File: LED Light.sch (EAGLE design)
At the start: 17 parts, among them J1 AVR_SPI_PRG_6NS, U1 Tiny85-20-SMT

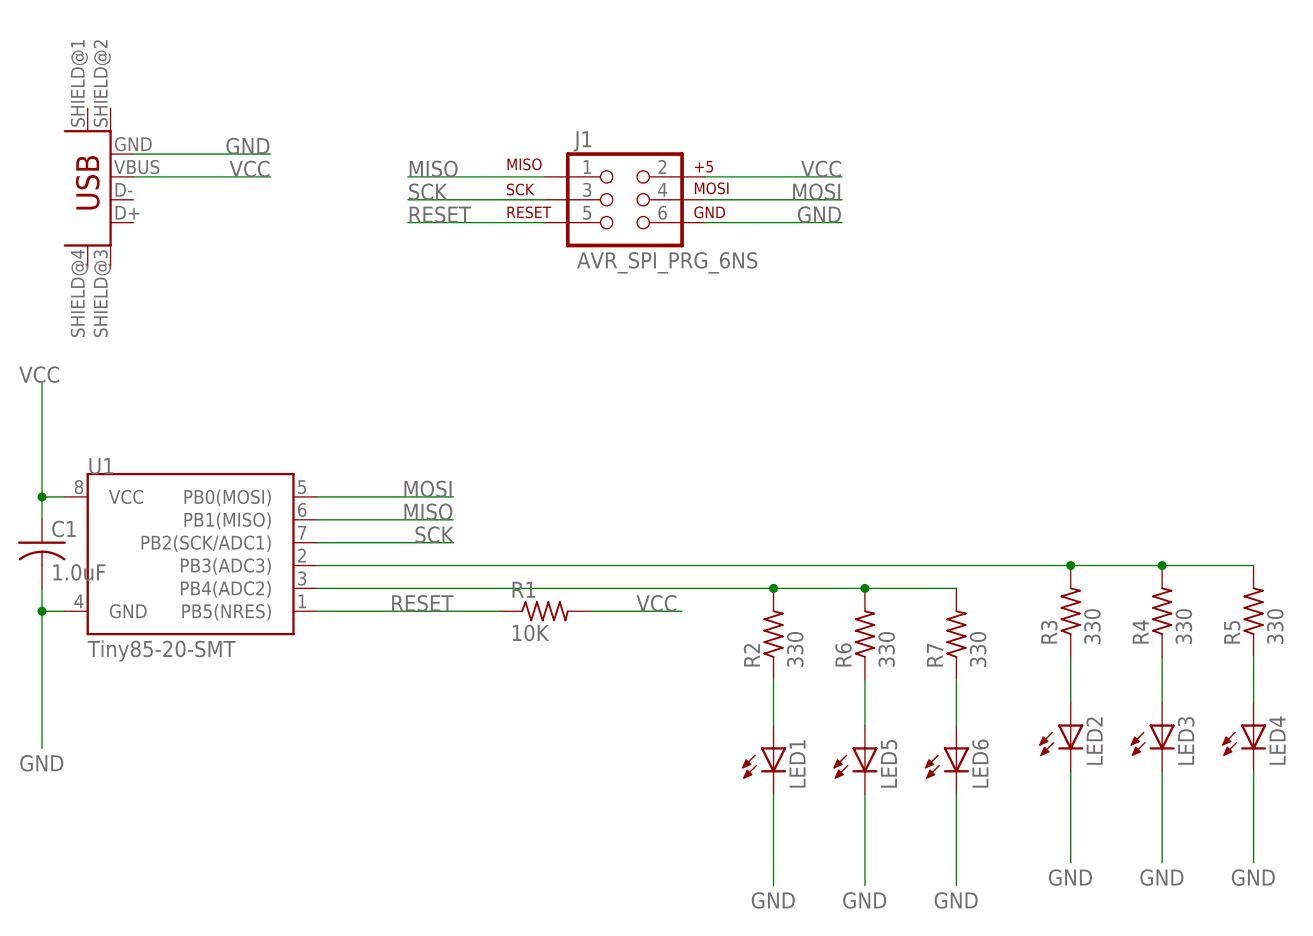
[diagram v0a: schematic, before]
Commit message: Light-bulb-shaped board, reverse-mount LEDs, and SMT AVR ISP header.
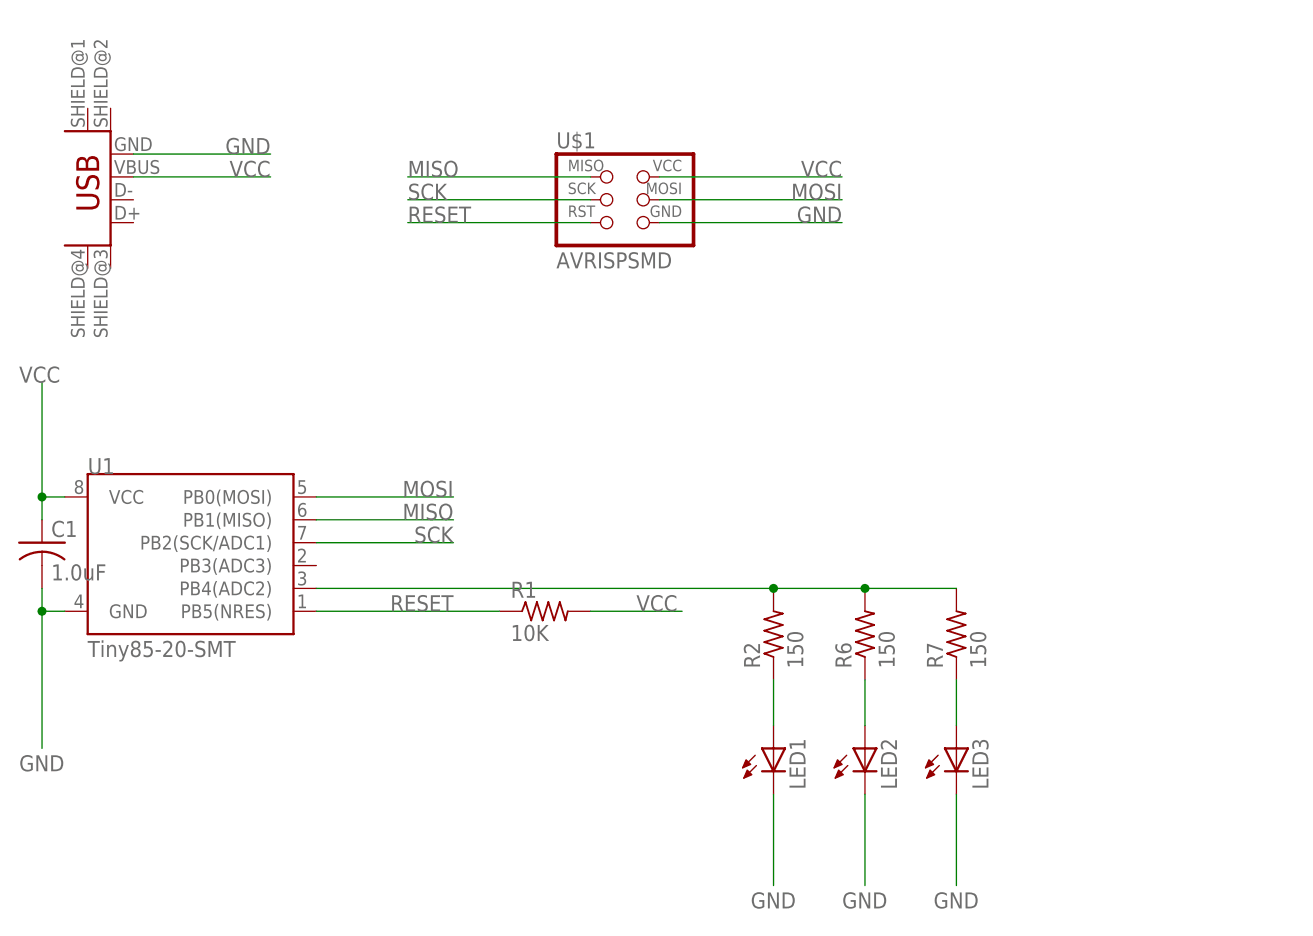
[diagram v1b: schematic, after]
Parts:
- removed J1: AVR_SPI_PRG_6NS, SparkFun-Connectors:AVR_SPI_PRG_6NS
- removed LED4, LED5, LED6: (no value), led:LEDSMT1206
- removed R3, R4, R5: 330, rcl:R-US_R1206
- added U$1: AVRISPSMD, fab:AVRISPSMD
- LED1, LED2, LED3: device led:LEDSMT1206 -> led:LEDTOPLED-SANTANA
- R2, R6, R7: value 330 -> 150
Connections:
- removed net N$2: R3.2, R4.2, R5.2, U1.PB3(ADC3)
- removed net N$4: LED2.A, R3.1
- removed net N$7: LED3.A, R4.1
- removed net N$8: LED4.A, R5.1
- net GND: now also U$1.GND; no longer J1.6, LED4.C, LED5.C, LED6.C
- net MISO: now also U$1.MISO; no longer J1.1
- net MOSI: now also U$1.MOSI; no longer J1.4
- net N$5: now also LED3.A; no longer LED6.A
- net N$6: now also LED2.A; no longer LED5.A
- net RESET: now also U$1.RST; no longer J1.5
- net SCK: now also U$1.SCK; no longer J1.3
- net VCC: now also U$1.VCC; no longer J1.2
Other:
- moved on the sheet: LED2, LED3
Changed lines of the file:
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@@
 <parts>
 <part name="U1" library="SparkFun-DigitalIC" deviceset="ATTINY45" device="TINY85-20-SMT" value="Tiny85-20-SMT"/>
-<part name="J1" library="SparkFun-Connectors" deviceset="AVR_SPI_PRG_6" device="NS"/>
 <part name="R1" library="rcl" deviceset="R-US_" device="R1206" value="10K"/>
-<part name="R2" library="rcl" deviceset="R-US_" device="R1206" value="330"/>
-<part name="R3" library="rcl" deviceset="R-US_" device="R1206" value="330"/>
-<part name="LED1" library="led" deviceset="LED" device="SMT1206"/>
-<part name="LED2" library="led" deviceset="LED" device="SMT1206"/>
+<part name="R2" library="rcl" deviceset="R-US_" device="R1206" value="150"/>
 <part name="JP1" library="fab" deviceset="USB_MINIB" device=""/>
 <part name="C1" library="rcl" deviceset="C-US" device="C1206" value="1.0uF"/>
-<part name="R4" library="rcl" deviceset="R-US_" device="R1206" value="330"/>
-<part name="LED3" library="led" deviceset="LED" device="SMT1206"/>
-<part name="R5" library="rcl" deviceset="R-US_" device="R1206" value="330"/>
-<part name="LED4" library="led" deviceset="LED" device="SMT1206"/>
-<part name="R6" library="rcl" deviceset="R-US_" device="R1206" value="330"/>
-<part name="R7" library="rcl" deviceset="R-US_" device="R1206" value="330"/>
-<part name="LED5" library="led" deviceset="LED" device="SMT1206"/>
-<part name="LED6" library="led" deviceset="LED" device="SMT1206"/>
+<part name="R6" library="rcl" deviceset="R-US_" device="R1206" value="150"/>
+<part name="R7" library="rcl" deviceset="R-US_" device="R1206" value="150"/>
+<part name="LED1" library="led" deviceset="LED" device="TOPLED-SANTANA"/>
+<part name="LED2" library="led" deviceset="LED" device="TOPLED-SANTANA"/>
+<part name="LED3" library="led" deviceset="LED" device="TOPLED-SANTANA"/>
+<part name="U$1" library="fab" deviceset="AVRISP" device="SMD"/>
 </parts>
 <sheets>
@@
 <instances>
 <instance part="U1" gate="G$1" x="27.94" y="38.1"/>
-<instance part="J1" gate="G$1" x="73.66" y="78.74"/>
 <instance part="R1" gate="G$1" x="66.04" y="33.02"/>
 <instance part="R2" gate="G$1" x="91.44" y="30.48" rot="R90"/>
-<instance part="R3" gate="G$1" x="124.46" y="33.02" rot="R90"/>
-<instance part="LED1" gate="G$1" x="91.44" y="17.78"/>
-<instance part="LED2" gate="G$1" x="124.46" y="20.32"/>
 <instance part="JP1" gate="G$1" x="17.78" y="78.74" rot="R180"/>
 <instance part="C1" gate="G$1" x="10.16" y="40.64"/>
-<instance part="R4" gate="G$1" x="134.62" y="33.02" rot="R90"/>
-<instance part="LED3" gate="G$1" x="134.62" y="20.32"/>
-<instance part="R5" gate="G$1" x="144.78" y="33.02" rot="R90"/>
-<instance part="LED4" gate="G$1" x="144.78" y="20.32"/>
 <instance part="R6" gate="G$1" x="101.6" y="30.48" rot="R90"/>
 <instance part="R7" gate="G$1" x="111.76" y="30.48" rot="R90"/>
-<instance part="LED5" gate="G$1" x="101.6" y="17.78"/>
-<instance part="LED6" gate="G$1" x="111.76" y="17.78"/>
+<instance part="LED1" gate="G$1" x="91.44" y="17.78"/>
+<instance part="LED2" gate="G$1" x="101.6" y="17.78"/>
+<instance part="LED3" gate="G$1" x="111.76" y="17.78"/>
+<instance part="U$1" gate="G$1" x="73.66" y="78.74"/>
 </instances>
 <busses>
@@
 <net name="VCC" class="0">
 <segment>
-<pinref part="J1" gate="G$1" pin="2"/>
-<wire x1="83.82" y1="81.28" x2="99.06" y2="81.28" width="0.1524" layer="91"/>
+<wire x1="78.74" y1="81.28" x2="99.06" y2="81.28" width="0.1524" layer="91"/>
 <label x="99.06" y="81.28" size="1.778" layer="95" rot="MR0"/>
+<pinref part="U$1" gate="G$1" pin="VCC"/>
 </segment>
 <segment>
@@
 <net name="MOSI" class="0">
 <segment>
-<pinref part="J1" gate="G$1" pin="4"/>
-<wire x1="83.82" y1="78.74" x2="99.06" y2="78.74" width="0.1524" layer="91"/>
+<wire x1="78.74" y1="78.74" x2="99.06" y2="78.74" width="0.1524" layer="91"/>
 <label x="99.06" y="78.74" size="1.778" layer="95" rot="MR0"/>
+<pinref part="U$1" gate="G$1" pin="MOSI"/>
 </segment>
 <segment>
@@
 <net name="GND" class="0">
 <segment>
-<pinref part="J1" gate="G$1" pin="6"/>
-<wire x1="83.82" y1="76.2" x2="99.06" y2="76.2" width="0.1524" layer="91"/>
+<wire x1="78.74" y1="76.2" x2="99.06" y2="76.2" width="0.1524" layer="91"/>
 <label x="99.06" y="76.2" size="1.778" layer="95" rot="MR0"/>
+<pinref part="U$1" gate="G$1" pin="GND"/>
 </segment>
 <segment>
@@
 </segment>
 <segment>
-<pinref part="LED1" gate="G$1" pin="C"/>
 <wire x1="91.44" y1="12.7" x2="91.44" y2="2.54" width="0.1524" layer="91"/>
 <label x="88.9" y="0" size="1.778" layer="95"/>
+<pinref part="LED1" gate="G$1" pin="C"/>
 </segment>
 <segment>
+<wire x1="101.6" y1="12.7" x2="101.6" y2="2.54" width="0.1524" layer="91"/>
+<label x="99.06" y="0" size="1.778" layer="95"/>
 <pinref part="LED2" gate="G$1" pin="C"/>
-<wire x1="124.46" y1="15.24" x2="124.46" y2="5.08" width="0.1524" layer="91"/>
-<label x="121.92" y="2.54" size="1.778" layer="95"/>
 </segment>
 <segment>
-<pinref part="LED3" gate="G$1" pin="C"/>
-<wire x1="134.62" y1="15.24" x2="134.62" y2="5.08" width="0.1524" layer="91"/>
-<label x="132.08" y="2.54" size="1.778" layer="95"/>
-</segment>
-<segment>
-<pinref part="LED4" gate="G$1" pin="C"/>
-<wire x1="144.78" y1="15.24" x2="144.78" y2="5.08" width="0.1524" layer="91"/>
-<label x="142.24" y="2.54" size="1.778" layer="95"/>
-</segment>
-<segment>
-<pinref part="LED5" gate="G$1" pin="C"/>
-<wire x1="101.6" y1="12.7" x2="101.6" y2="2.54" width="0.1524" layer="91"/>
-<label x="99.06" y="0" size="1.778" layer="95"/>
-</segment>
-<segment>
-<pinref part="LED6" gate="G$1" pin="C"/>
 <wire x1="111.76" y1="12.7" x2="111.76" y2="2.54" width="0.1524" layer="91"/>
 <label x="109.22" y="0" size="1.778" layer="95"/>
+<pinref part="LED3" gate="G$1" pin="C"/>
 </segment>
 </net>
 <net name="RESET" class="0">
 <segment>
-<pinref part="J1" gate="G$1" pin="5"/>
-<wire x1="66.04" y1="76.2" x2="50.8" y2="76.2" width="0.1524" layer="91"/>
+<wire x1="71.12" y1="76.2" x2="50.8" y2="76.2" width="0.1524" layer="91"/>
 <label x="50.8" y="76.2" size="1.778" layer="95"/>
+<pinref part="U$1" gate="G$1" pin="RST"/>
 </segment>
 <segment>
@@
 <net name="SCK" class="0">
 <segment>
-<pinref part="J1" gate="G$1" pin="3"/>
-<wire x1="66.04" y1="78.74" x2="50.8" y2="78.74" width="0.1524" layer="91"/>
+<wire x1="71.12" y1="78.74" x2="50.8" y2="78.74" width="0.1524" layer="91"/>
 <label x="50.8" y="78.74" size="1.778" layer="95"/>
+<pinref part="U$1" gate="G$1" pin="SCK"/>
 </segment>
 <segment>
@@
 <net name="MISO" class="0">
 <segment>
-<pinref part="J1" gate="G$1" pin="1"/>
-<wire x1="66.04" y1="81.28" x2="50.8" y2="81.28" width="0.1524" layer="91"/>
+<wire x1="71.12" y1="81.28" x2="50.8" y2="81.28" width="0.1524" layer="91"/>
 <label x="50.8" y="81.28" size="1.778" layer="95"/>
+<pinref part="U$1" gate="G$1" pin="MISO"/>
 </segment>
 <segment>
@@
 </segment>
 </net>
-<net name="N$2" class="0">
-<segment>
-<pinref part="U1" gate="G$1" pin="PB3(ADC3)"/>
-<wire x1="40.64" y1="38.1" x2="124.46" y2="38.1" width="0.1524" layer="91"/>
-<pinref part="R3" gate="G$1" pin="2"/>
-<pinref part="R4" gate="G$1" pin="2"/>
-<wire x1="124.46" y1="38.1" x2="134.62" y2="38.1" width="0.1524" layer="91"/>
-<junction x="124.46" y="38.1"/>
-<pinref part="R5" gate="G$1" pin="2"/>
-<wire x1="134.62" y1="38.1" x2="144.78" y2="38.1" width="0.1524" layer="91"/>
-<junction x="134.62" y="38.1"/>
-</segment>
-</net>
 <net name="N$3" class="0">
 <segment>
 <pinref part="R2" gate="G$1" pin="1"/>
+<wire x1="91.44" y1="20.32" x2="91.44" y2="25.4" width="0.1524" layer="91"/>
 <pinref part="LED1" gate="G$1" pin="A"/>
-<wire x1="91.44" y1="20.32" x2="91.44" y2="25.4" width="0.1524" layer="91"/>
-</segment>
-</net>
-<net name="N$4" class="0">
-<segment>
-<pinref part="R3" gate="G$1" pin="1"/>
-<pinref part="LED2" gate="G$1" pin="A"/>
-<wire x1="124.46" y1="22.86" x2="124.46" y2="27.94" width="0.1524" layer="91"/>
-</segment>
-</net>
-<net name="N$7" class="0">
-<segment>
-<pinref part="R4" gate="G$1" pin="1"/>
-<pinref part="LED3" gate="G$1" pin="A"/>
-<wire x1="134.62" y1="27.94" x2="134.62" y2="22.86" width="0.1524" layer="91"/>
-</segment>
-</net>
-<net name="N$8" class="0">
-<segment>
-<pinref part="R5" gate="G$1" pin="1"/>
-<pinref part="LED4" gate="G$1" pin="A"/>
-<wire x1="144.78" y1="27.94" x2="144.78" y2="22.86" width="0.1524" layer="91"/>
 </segment>
 </net>
@@
 <segment>
 <pinref part="R7" gate="G$1" pin="1"/>
-<pinref part="LED6" gate="G$1" pin="A"/>
 <wire x1="111.76" y1="25.4" x2="111.76" y2="20.32" width="0.1524" layer="91"/>
+<pinref part="LED3" gate="G$1" pin="A"/>
 </segment>
 </net>
@@
 <segment>
 <pinref part="R6" gate="G$1" pin="1"/>
-<pinref part="LED5" gate="G$1" pin="A"/>
 <wire x1="101.6" y1="25.4" x2="101.6" y2="20.32" width="0.1524" layer="91"/>
+<pinref part="LED2" gate="G$1" pin="A"/>
 </segment>
 </net>

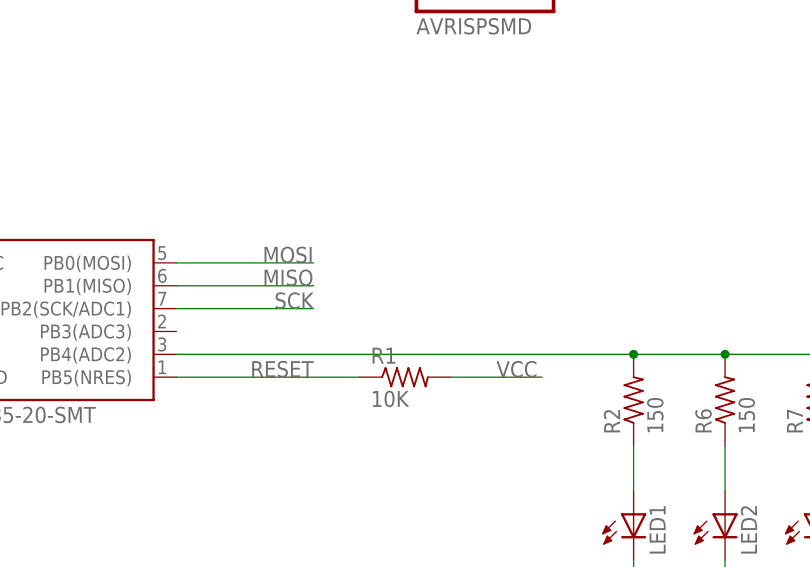
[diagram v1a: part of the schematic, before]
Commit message: Add 10M resistor and traces for capacitive sensing.
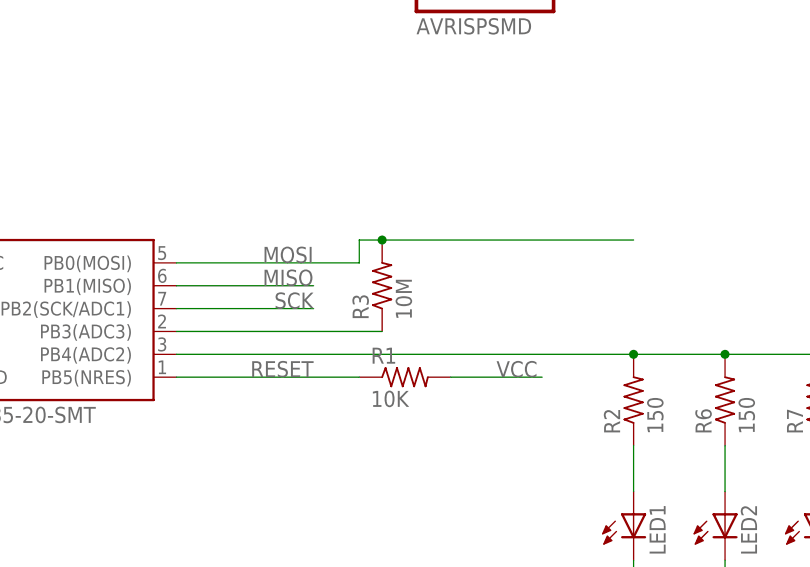
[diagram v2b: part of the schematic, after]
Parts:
- added R3: 10M, rcl:R-US_R1206
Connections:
- new net N$2: R3.1, U1.PB3(ADC3)
- net MOSI: now also R3.2
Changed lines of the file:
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@@
 <part name="LED3" library="led" deviceset="LED" device="TOPLED-SANTANA"/>
 <part name="U$1" library="fab" deviceset="AVRISP" device="SMD"/>
+<part name="R3" library="rcl" deviceset="R-US_" device="R1206" value="10M"/>
 </parts>
 <sheets>
@@
 <instance part="LED3" gate="G$1" x="111.76" y="17.78"/>
 <instance part="U$1" gate="G$1" x="73.66" y="78.74"/>
+<instance part="R3" gate="G$1" x="63.5" y="43.18" rot="R90"/>
 </instances>
 <busses>
@@
 <segment>
 <pinref part="U1" gate="G$1" pin="PB0(MOSI)"/>
-<wire x1="40.64" y1="45.72" x2="55.88" y2="45.72" width="0.1524" layer="91"/>
+<wire x1="40.64" y1="45.72" x2="60.96" y2="45.72" width="0.1524" layer="91"/>
 <label x="55.88" y="45.72" size="1.778" layer="95" rot="MR0"/>
+<wire x1="60.96" y1="45.72" x2="60.96" y2="48.26" width="0.1524" layer="91"/>
+<pinref part="R3" gate="G$1" pin="2"/>
+<wire x1="60.96" y1="48.26" x2="63.5" y2="48.26" width="0.1524" layer="91"/>
+<wire x1="63.5" y1="48.26" x2="91.44" y2="48.26" width="0.1524" layer="91"/>
+<junction x="63.5" y="48.26"/>
 </segment>
 </net>
@@
 </segment>
 </net>
+<net name="N$2" class="0">
+<segment>
+<pinref part="U1" gate="G$1" pin="PB3(ADC3)"/>
+<pinref part="R3" gate="G$1" pin="1"/>
+<wire x1="63.5" y1="38.1" x2="40.64" y2="38.1" width="0.1524" layer="91"/>
+</segment>
+</net>
